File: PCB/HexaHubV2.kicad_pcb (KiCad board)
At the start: 2 copper layers, 90 x 52.5 mm, 29 parts, among them J1 USB_C_Receptacle_USB2.0_16P, J2 USB_A, J3 USB_A, J4 USB_A, J5 USB_A, U1 SL2.1A, Y1 12MHz

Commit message: Slight changes to PCB and updated gerbers
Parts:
- F2, F3, F4, F5: value 2A -> 500mA
- renumbered C9 to C5, C10 to C6, C11 to C7, C12 to C8
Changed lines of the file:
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@@
 		(descr "Capacitor SMD 0402 (1005 Metric), square (rectangular) end terminal, IPC-7351 nominal, (Body size source: IPC-SM-782 page 76, https://www.pcb-3d.com/wordpress/wp-content/uploads/ipc-sm-782a_amendment_1_and_2.pdf)")
 		(tags "capacitor")
-		(property "Reference" "C11"
+		(property "Reference" "C7"
 			(at 0 2 180)
 			(layer "F.SilkS")
@@
 		(descr "<b>Small Outline package</b> 150 mil")
 		(property "Reference" "U1"
-			(at -6.096 0 0)
+			(at -7 0 0)
 			(layer "F.SilkS")
 			(effects
@@
 			)
 		)
-		(property "Value" "2A"
+		(property "Value" "500mA"
 			(at 0 1.83 0)
 			(layer "F.Fab")
@@
 		(descr "Capacitor SMD 0603 (1608 Metric), square (rectangular) end terminal, IPC-7351 nominal, (Body size source: IPC-SM-782 page 76, https://www.pcb-3d.com/wordpress/wp-content/uploads/ipc-sm-782a_amendment_1_and_2.pdf)")
 		(tags "capacitor")
-		(property "Reference" "C10"
+		(property "Reference" "C6"
 			(at -3.775 0 90)
 			(layer "F.SilkS")
@@
 		(descr "Capacitor SMD 0402 (1005 Metric), square (rectangular) end terminal, IPC-7351 nominal, (Body size source: IPC-SM-782 page 76, https://www.pcb-3d.com/wordpress/wp-content/uploads/ipc-sm-782a_amendment_1_and_2.pdf)")
 		(tags "capacitor")
-		(property "Reference" "C12"
+		(property "Reference" "C8"
 			(at 3 0 90)
 			(layer "F.SilkS")
@@
 			)
 		)
-		(property "Value" "2A"
+		(property "Value" "500mA"
 			(at 0 1.83 0)
 			(layer "F.Fab")
@@
 		(descr "Capacitor SMD 0603 (1608 Metric), square (rectangular) end terminal, IPC-7351 nominal, (Body size source: IPC-SM-782 page 76, https://www.pcb-3d.com/wordpress/wp-content/uploads/ipc-sm-782a_amendment_1_and_2.pdf)")
 		(tags "capacitor")
-		(property "Reference" "C9"
+		(property "Reference" "C5"
 			(at -3.75 0 90)
 			(layer "F.SilkS")
@@
 			)
 		)
-		(property "Value" "2A"
+		(property "Value" "500mA"
 			(at 0 1.83 0)
 			(layer "F.Fab")
@@
 			)
 		)
-		(property "Value" "2A"
+		(property "Value" "500mA"
 			(at 0 1.829999 90)
 			(layer "F.Fab")

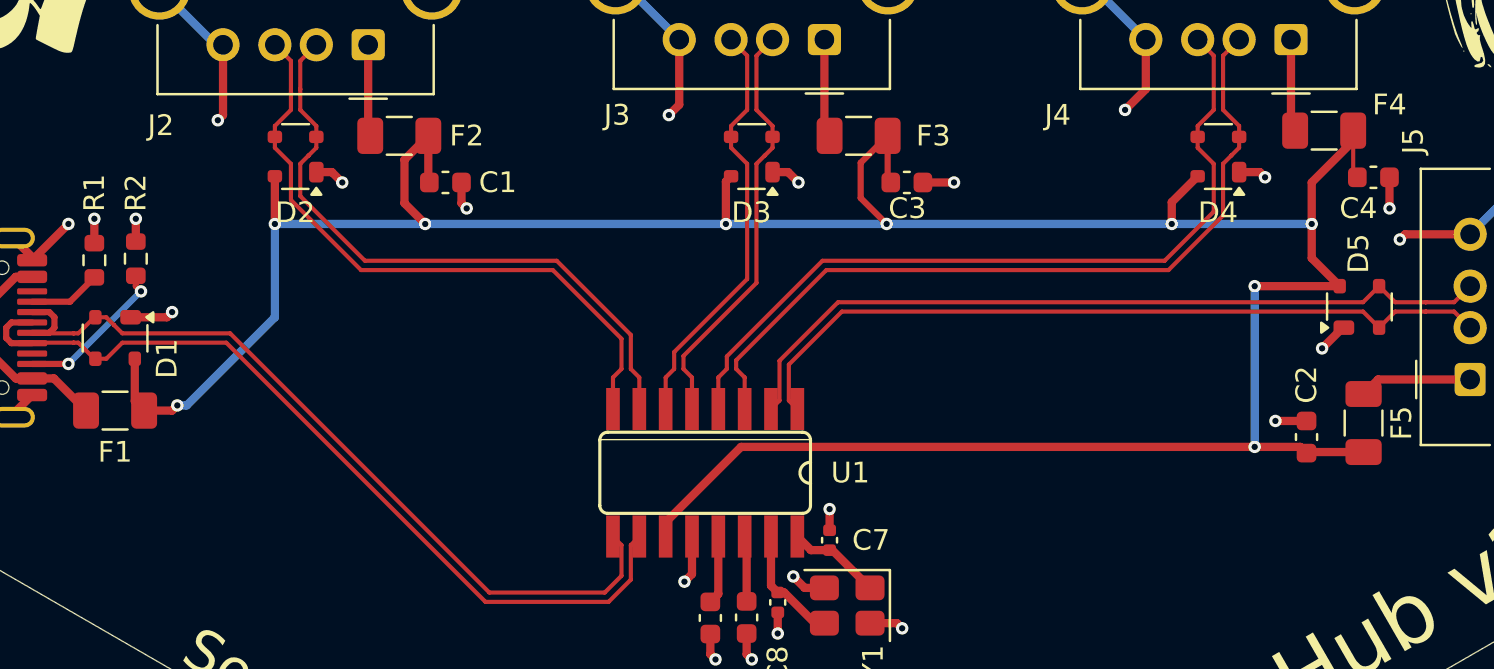
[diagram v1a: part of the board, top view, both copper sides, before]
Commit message: Slight changes to PCB
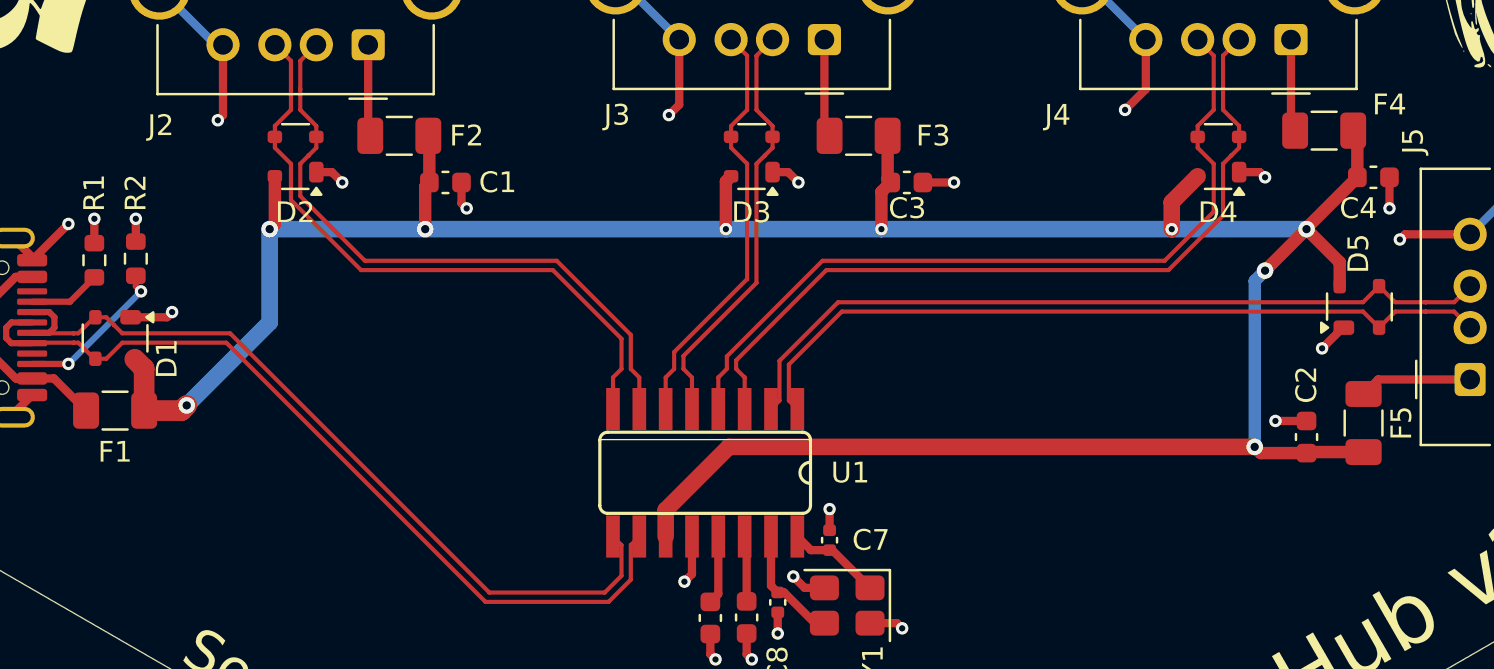
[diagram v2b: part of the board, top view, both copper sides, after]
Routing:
- net +5V: track 147.0 -> 139.8 mm
